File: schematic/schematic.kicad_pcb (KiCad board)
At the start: 4 copper layers, 77.8 x 81.6 mm, 154 parts, among them IC1 RS0108YQ20, IC2 AS312, IC3 TPS630250RNCR, IC4 SIM7600G-H_R2, J1 SIM7155-6-1-14-A, J3 USB_C_Receptacle_USB2.0, J9 BATT_CONNECTOR, Q1 BC817, Q10 MMBT3904, Q11 MMBT3904, Q15 SI2302, Q16 SI2302, Q8 NCE6005AR, Q9 NCE6005AR, U10 TPS56339DDC, U2 MT3608, U3 AM2302, U4 TP4056, U6 ESP32-WROOM-32, U8 CH340T(SSOP20W), Y1 12MHz

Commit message: MORE Routing
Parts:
- removed R97: 4.7k, Resistor_SMD:R_0402_1005Metric
- C72, R111, R19: moved to B.Cu
- moved D11 2.07 mm to (117.0, 66.8)
- moved D10 1.84 mm to (117.2, 63.8)
- moved C71 0.71 mm to (108.0, 91.0)
- moved C72 0.60 mm to (116.0, 90.7)
- moved R19 0.39 mm to (113.1, 64.8)
- moved R82 0.37 mm to (108.1, 89.6)
- moved R110 0.25 mm to (108.2, 87.8), turned to 0 degrees
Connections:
- IC1 pad 13: /SIM808_GPRS_GPS_MODULE/IO33 -> IO33
- IC1 pad 14: /SIM808_GPRS_GPS_MODULE/IO34 -> IO34
- IC1 pad 15: /SIM808_GPRS_GPS_MODULE/IO32 -> IO32
- IC1 pad 16: /SIM808_GPRS_GPS_MODULE/IO25 -> IO25
- IC1 pad 17: /SIM808_GPRS_GPS_MODULE/IO27 -> IO27
- IC1 pad 18: /SIM808_GPRS_GPS_MODULE/IO26 -> IO26
- U6 pad 10: /IO25 -> IO25
- U6 pad 11: /IO26 -> IO26
- U6 pad 12: /IO27 -> IO27
- U6 pad 6: /IO34 -> IO34
- U6 pad 8: /IO32 -> IO32
- U6 pad 9: /IO33 -> IO33
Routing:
- net IO4: track 0.00 -> 53.0 mm, vias 0 -> 2
- net /Motion_out: track 63.8 -> 14.8 mm
- net /SIM808_GPRS_GPS_MODULE/Flight: track 0.00 -> 46.2 mm, vias 0 -> 2
- net IO33: track 0.00 -> 41.1 mm, vias 0 -> 2
- net IO34: track 0.00 -> 41.0 mm, vias 0 -> 3
- net IO27: track 0.00 -> 32.6 mm, vias 0 -> 2
- net /SIM808_GPRS_GPS_MODULE/RI: track 0.00 -> 31.6 mm, vias 0 -> 2
- net IO25: track 0.00 -> 31.0 mm, vias 0 -> 2
- net IO32: track 0.00 -> 30.6 mm, vias 0 -> 2
- net IO26: track 0.00 -> 29.0 mm, vias 0 -> 2
- net /boot: track 4.29 -> 33.2 mm, vias 0 -> 2
- net /SIM808_GPRS_GPS_MODULE/DTR: track 0.00 -> 28.3 mm, vias 0 -> 2
- net /SIM808_GPRS_GPS_MODULE/LED_Status: track 36.8 -> 59.4 mm, vias 1 -> 3
- net +3V3: track 177.3 -> 155.2 mm, vias 8 -> 7
- net /switch: track 46.7 -> 25.2 mm, vias 2 -> 1
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
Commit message: Ground and power routing
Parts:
- removed J9: BATT_CONNECTOR, TerminalBlock_Phoenix:TerminalBlock_Phoenix_PTSM-0,5-2-HV-2.5-SMD_1x02-1MP_P2.50mm_Vertical
- moved BAT-1 15.0 mm to (151.9, 125.9)
- moved BAT+1 12.0 mm to (158.2, 125.9)
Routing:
- net /Motion_out: track 14.8 -> 68.9 mm, vias 1 -> 2
- net /red: track 9.58 -> 41.6 mm, vias 1 -> 2
- net /blue: track 9.74 -> 37.6 mm, vias 1 -> 2
- net /green: track 9.60 -> 33.1 mm, vias 1 -> 2
- net GND: track 388.3 -> 407.5 mm, vias 241 -> 251
- net /DHT22_Data: track 70.5 -> 87.9 mm, vias 0 -> 2
- net +3V3: track 155.2 -> 171.5 mm
- net /switch: track 25.2 -> 33.8 mm, vias 1 -> 2
- net +BATT: track 103.7 -> 107.8 mm
- net /IO2: track 20.0 -> 23.0 mm

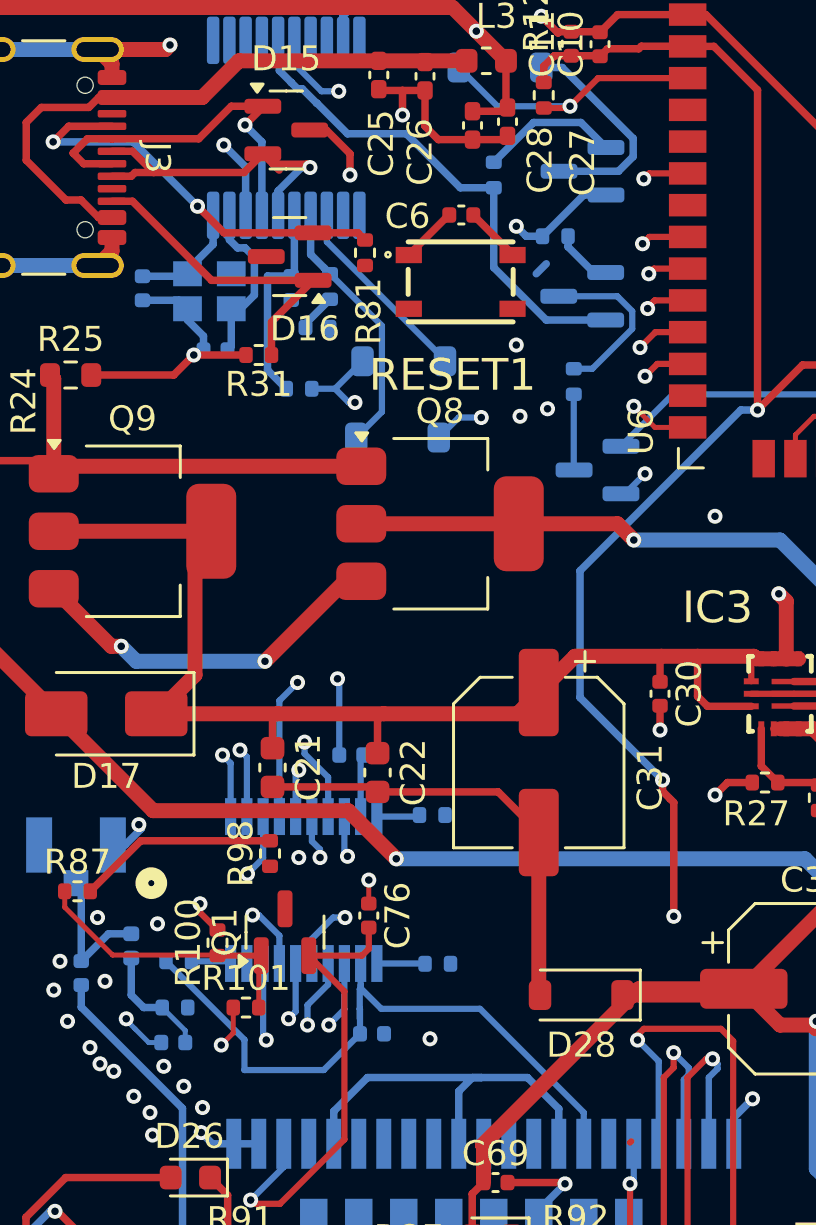
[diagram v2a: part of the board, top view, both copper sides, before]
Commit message: Ground and power routing
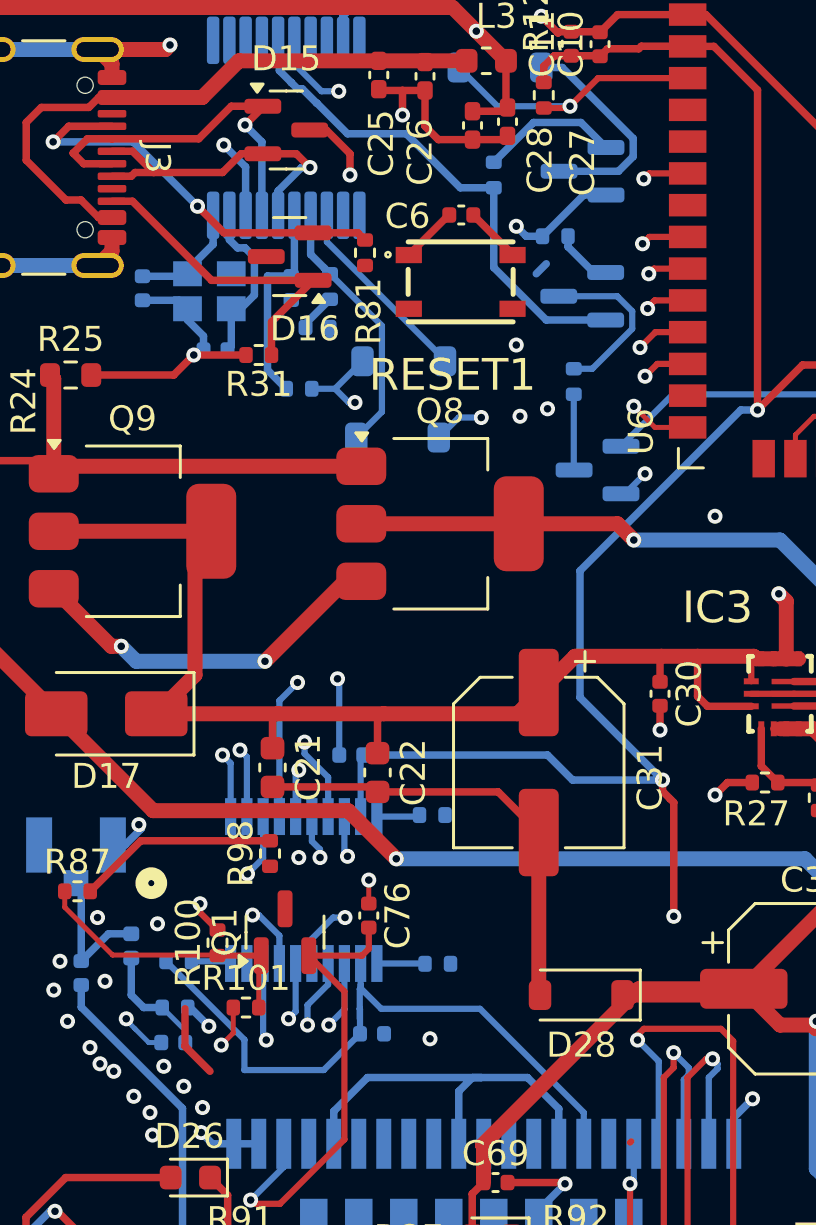
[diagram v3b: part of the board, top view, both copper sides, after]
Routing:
- net +3V3: track 171.5 -> 208.2 mm, vias 7 -> 8
- net (no net): track 0.00 -> 2.91 mm
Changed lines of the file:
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@@
 		)
 	)
+	(segment
+		(start 108.5 91.15)
+		(end 109.5 92.15)
+		(width 0.3)
+		(layer "F.Cu")
+		(net 0)
+	)
+	(segment
+		(start 108.5 89.65)
+		(end 108.5 91.15)
+		(width 0.3)
+		(layer "F.Cu")
+		(net 0)
+	)
 	(via
 		(at 145.5 123.35)
@@
 	)
 	(via
+		(at 109.453058 90.346942)
+		(size 0.6)
+		(drill 0.3)
+		(layers "F.Cu" "B.Cu")
+		(net 3)
+	)
+	(via
 		(at 160.05 87.75)
 		(size 0.6)
@@
 	)
 	(segment
+		(start 108.61 89.6)
+		(end 108.706116 89.6)
+		(width 0.3)
+		(layer "B.Cu")
+		(net 3)
+	)
+	(segment
 		(start 165.034 122.014)
 		(end 166.45 123.43)
@@
 	)
 	(segment
+		(start 124 80.5)
+		(end 123 79.5)
+		(width 0.3)
+		(layer "B.Cu")
+		(net 3)
+	)
+	(segment
 		(start 160.05 87.75)
 		(end 164.55 92.25)
@@
 	)
 	(segment
+		(start 108.706116 89.6)
+		(end 109.453058 90.346942)
+		(width 0.3)
+		(layer "B.Cu")
+		(net 3)
+	)
+	(segment
 		(start 160.05 87.75)
 		(end 148.3 76)
@@
 	)
 	(segment
+		(start 123 79.5)
+		(end 115.63 79.5)
+		(width 0.3)
+		(layer "B.Cu")
+		(net 3)
+	)
+	(segment
+		(start 127.6 80.5)
+		(end 124 80.5)
+		(width 0.3)
+		(layer "B.Cu")
+		(net 3)
+	)
+	(segment
 		(start 165.034 105.196)
 		(end 165.034 122.014)
@@
 	)
 	(segment
+		(start 127.349 85.249)
+		(end 110.930346 85.249)
+		(width 0.3)
+		(layer "In2.Cu")
+		(net 3)
+	)
+	(segment
+		(start 128.05 85.95)
+		(end 127.349 85.249)
+		(width 0.3)
+		(layer "In2.Cu")
+		(net 3)
+	)
+	(segment
+		(start 109.453058 86.726288)
+		(end 109.453058 90.346942)
+		(width 0.3)
+		(layer "In2.Cu")
+		(net 3)
+	)
+	(segment
+		(start 110.930346 85.249)
+		(end 109.453058 86.726288)
+		(width 0.3)
+		(layer "In2.Cu")
+		(net 3)
+	)
+	(segment
 		(start 128.605 52.425)
 		(end 125.024 52.425)
@@
 	)
 	(segment
-		(start 113.36875 55.86875)
-		(end 113.5 56)
-		(width 0.3)
-		(layer "F.Cu")
-		(net 19)
-	)
-	(segment
 		(start 106.35 56.35)
 		(end 106.5 56.2)
@@
 	)
 	(segment
-		(start 106.4 55.35)
-		(end 107.25 56.2)
+		(start 107.25 56.2)
+		(end 110 56.2)
 		(width 0.3)
 		(layer "F.Cu")
@@
 	)
 	(segment
-		(start 112.03125 55.86875)
-		(end 113.36875 55.86875)
+		(start 106.4 55.35)
+		(end 107.25 56.2)
 		(width 0.3)
 		(layer "F.Cu")
@@
 	)
 	(segment
-		(start 107.25 56.2)
-		(end 110.8625 56.2)
+		(start 110.75 55.45)
+		(end 111.6125 55.45)
 		(width 0.3)
 		(layer "F.Cu")
@@
 	)
 	(segment
-		(start 112.266034 56.103534)
-		(end 112.03125 55.86875)
+		(start 106.5 56.2)
+		(end 107.25 56.2)
 		(width 0.3)
 		(layer "F.Cu")
@@
 	)
 	(segment
-		(start 106.5 56.2)
-		(end 107.25 56.2)
+		(start 105.58 55.35)
+		(end 106.4 55.35)
 		(width 0.3)
 		(layer "F.Cu")
@@
 	)
 	(segment
-		(start 105.58 55.35)
-		(end 106.4 55.35)
+		(start 111.6125 55.45)
+		(end 112.95 55.45)
 		(width 0.3)
 		(layer "F.Cu")
@@
 	)
 	(segment
-		(start 112.03125 55.86875)
-		(end 111.6125 55.45)
+		(start 112.95 55.45)
+		(end 113.5 56)
 		(width 0.3)
 		(layer "F.Cu")
@@
 	)
 	(segment
-		(start 110.8625 56.2)
-		(end 111.6125 55.45)
+		(start 110 56.2)
+		(end 110.75 55.45)
 		(width 0.3)
 		(layer "F.Cu")
@@
 		(min_thickness 0.25)
 		(filled_areas_thickness no)
-		(fill
+		(fill yes
 			(thermal_gap 0.5)
 			(thermal_bridge_width 0.5)
@@
 		(min_thickness 0.25)
 		(filled_areas_thickness no)
-		(fill
+		(fill yes
 			(thermal_gap 0.5)
 			(thermal_bridge_width 0.5)
